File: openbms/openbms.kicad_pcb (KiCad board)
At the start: 4 copper layers, 68.4 x 52.4 mm, 210 parts, among them J1 3-pin JST connector, J2 TagConnect_TC2030, J3 8-pin JST connector, J4 2-pin JST connector, J5 XT60PW-M connector, J6 XT60PW-F connector, J7 7-pin JST connector, Q1 NTMFS5C612NLT1G, Q2 NTMFS5C612NLT1G, Q3 BSS84AKW,115, Q4 2N7002KW, Q5 2N7002KW, Q6 BSS84AKW,115, Q7 2N7002KW, U1 DMP68D1LVQ-7, U10 DMP68D1LVQ-7, U11 DMN601VK-7, U12 DMN601VK-7, U13 DMN601VK-7, U14 DMN601VK-7, U15 STM32L431CCUx, U16 TCAN3413DRBR, U17 32kbit EEPROM memory, U18 DMP68D1LVQ-7, U19 TPS12000QDGXRQ1, U2 DMP68D1LVQ-7, U20 LMZM23600V3, U3 DMN601VK-7, U4 DMP68D1LVQ-7, U5 ADS131M08xPBS, U6 DMP68D1LVQ-7, U7 DMN601VK-7, U8 DMP68D1LVQ-7, U9 DMP68D1LVQ-7, Y1 8.192MHz, Y2 8MHz

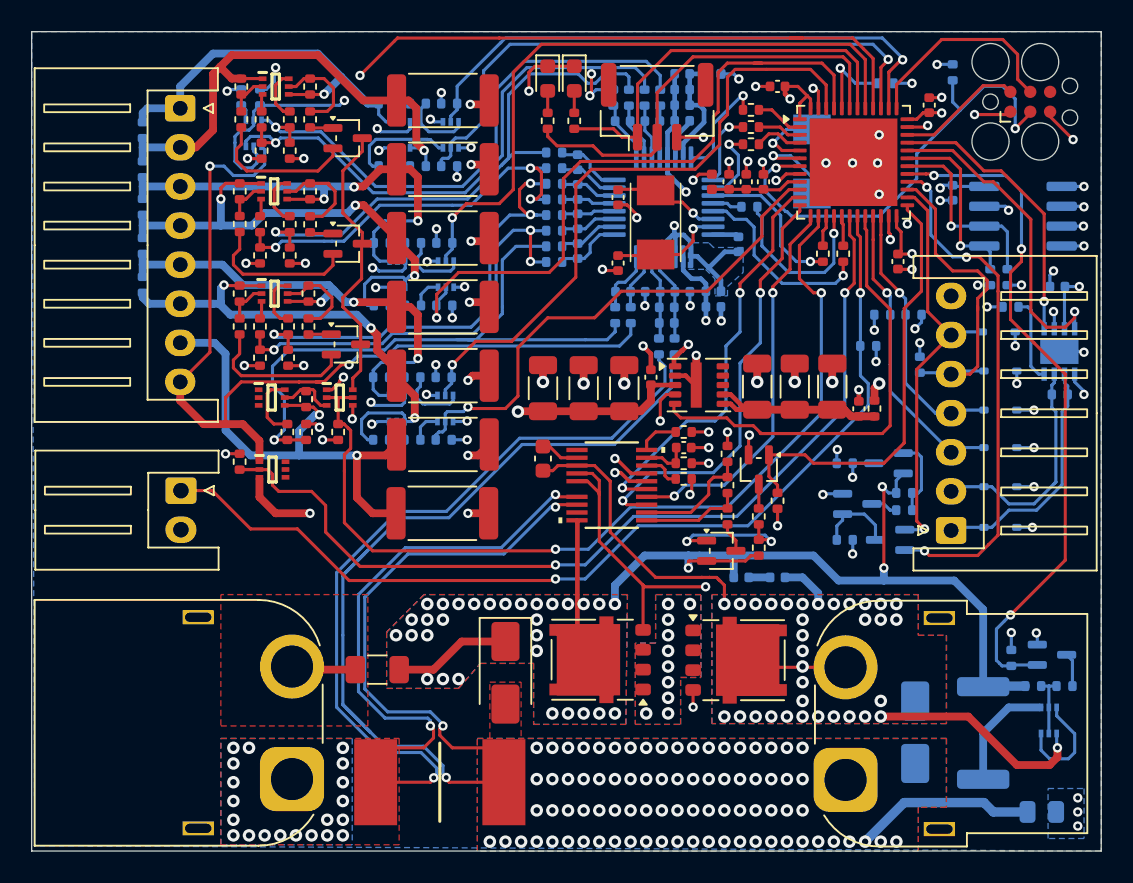
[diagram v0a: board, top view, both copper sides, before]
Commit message: Footprints for pmos/nmos and pmos/pmos packages fixed, charger detection added, pwr_gd and flt_gd lines removed
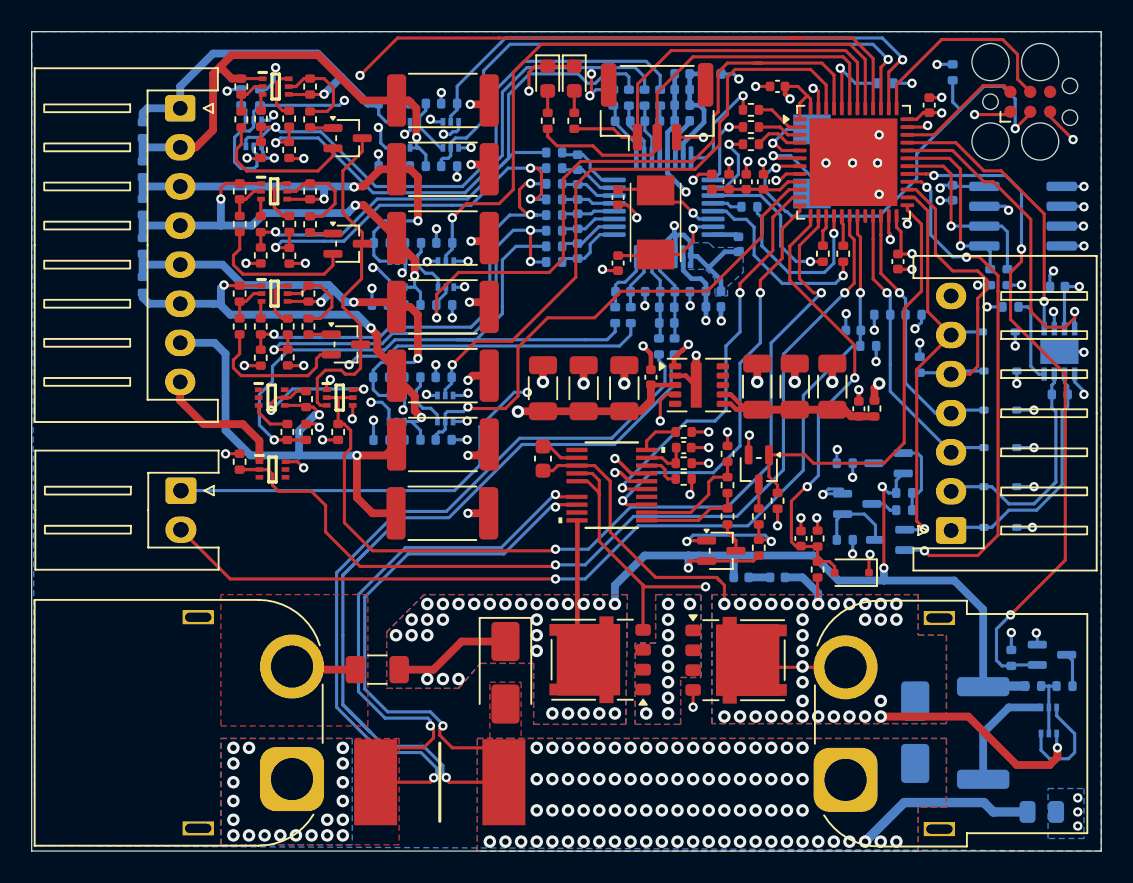
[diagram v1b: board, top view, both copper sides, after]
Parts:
- added C35: 10n, Capacitor_SMD:C_0402_1005Metric, B.Cu at (116.4, 53.3)
- added C44: 10n, Capacitor_SMD:C_0402_1005Metric, F.Cu at (113.0, 66.6)
- added D15: BAT54J, Diode_SMD:D_SOD-323F, F.Cu at (116.3, 68.8)
- added R116: 100k, Resistor_SMD:R_0402_1005Metric, F.Cu at (114.1, 68.6)
- added R118: 10k, Resistor_SMD:R_0402_1005Metric, F.Cu at (114.1, 66.6)
- Q1, Q2: footprint custom_library:ONSemi_SO-8FL_488AA -> Package_SO:ONSemi_SO-8FL_488AA
- U15: footprint custom_library:QFN-48-1EP_7x7mm_P0.5mm_EP5.6x5.6mm -> Package_DFN_QFN:QFN-48-1EP_7x7mm_P0.5mm_EP5.6x5.6mm
- U16: footprint custom_library:SON65P300X300X100-9N-D -> custom_library:TCAN3413DRBR
- U5: footprint custom_library:TQFP-32_5x5mm_P0.5mm -> Package_QFP:TQFP-32_5x5mm_P0.5mm
- moved R35 2.12 mm to (86.1, 51.7), turned to 0 degrees
- moved R63 2.00 mm to (88.2, 60.3), turned to 0 degrees
- moved R65 1.98 mm to (86.2, 60.4), turned to 0 degrees
- moved R31 1.96 mm to (88.2, 51.7), turned to 0 degrees
- moved R36 1.87 mm to (80.3, 48.6)
- moved R27 1.87 mm to (80.3, 46.5)
- moved R28 1.85 mm to (78.5, 46.5)
- moved R37 1.85 mm to (78.5, 48.5)
- moved R13 1.84 mm to (78.5, 39.8)
- moved R16 1.84 mm to (78.5, 41.8)
- moved R60 1.78 mm to (80.2, 55.1)
- moved R56 1.78 mm to (80.2, 53.1)
- moved R12 1.76 mm to (80.3, 39.8)
- moved R15 1.76 mm to (80.3, 41.8)
- moved R57 1.75 mm to (78.5, 53.1)
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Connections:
- net /Battery/BATT_PWR_VCC renamed /FETs/BATT_PWR_VCC
- J4 pad 1: /MCU/NTC -> +3V3
- J4 pad 2: GND -> /MCU/NTC
- R15 pad 1: GND -> GND_BATT_CELL
- R16 pad 1: GND -> GND_BATT_CELL
- R36 pad 1: GND -> GND_BATT_CELL
- R37 pad 1: GND -> GND_BATT_CELL
- R60 pad 1: GND -> GND_BATT_CELL
- R61 pad 1: GND -> GND_BATT_CELL
- R73 pad 1: GND -> GND_BATT_CELL
- R77 pad 1: GND -> GND_BATT_CELL
- U1 pad 3: Net-(R10-Pad2) -> Net-(R11-Pad2)
- U1 pad 6: Net-(R11-Pad2) -> Net-(R10-Pad2)
- U10 pad 3: unconnected-(U10-Pad3) -> Net-(R69-Pad2)
- U10 pad 6: Net-(R69-Pad2) -> unconnected-(U10-Pad6)
- U11 pad 3: Net-(R66-Pad2) -> Net-(D1-K)
- U11 pad 6: Net-(D1-K) -> Net-(R66-Pad2)
- U12 pad 3: Net-(R64-Pad1) -> Net-(R65-Pad1)
- U12 pad 6: Net-(R65-Pad1) -> Net-(R64-Pad1)
- U13 pad 3: Net-(R74-Pad1) -> unconnected-(U13-Pad3)
- U13 pad 6: unconnected-(U13-Pad6) -> Net-(R74-Pad1)
- U14 pad 3: /ADC/CELL_6_M -> /ADC/CELL_7_M
- U14 pad 6: /ADC/CELL_7_M -> /ADC/CELL_6_M
- U15 pad 13: /FETs/DRV_FLT_GD -> /FETs/CHG_PRES
- U15 pad 20: /MCU/PWR_PG -> unconnected-(U15-PB2-Pad20)
- U19 pad 4: /FETs/DRV_FLT_GD -> unconnected-(U19-FLT_GD-Pad4)
- U2 pad 3: Net-(R12-Pad2) -> Net-(R13-Pad2)
- U2 pad 6: Net-(R13-Pad2) -> Net-(R12-Pad2)
- U20 pad 5: /MCU/PWR_PG -> unconnected-(U20-PG-Pad5)
- U3 pad 3: Net-(R6-Pad1) -> Net-(R7-Pad1)
- U3 pad 6: Net-(R7-Pad1) -> Net-(R6-Pad1)
- U4 pad 3: Net-(R27-Pad2) -> Net-(R28-Pad2)
- U4 pad 6: Net-(R28-Pad2) -> Net-(R27-Pad2)
- U6 pad 3: Net-(R41-Pad2) -> Net-(R42-Pad2)
- U6 pad 6: Net-(R42-Pad2) -> Net-(R41-Pad2)
- U7 pad 3: Net-(R34-Pad1) -> Net-(R35-Pad1)
- U7 pad 6: Net-(R35-Pad1) -> Net-(R34-Pad1)
- U8 pad 3: Net-(R56-Pad2) -> Net-(R57-Pad2)
- U8 pad 6: Net-(R57-Pad2) -> Net-(R56-Pad2)
- U9 pad 3: Net-(R67-Pad2) -> Net-(R68-Pad2)
- U9 pad 6: Net-(R68-Pad2) -> Net-(R67-Pad2)
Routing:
- net +3V3: track 157.3 -> 200.9 mm, vias 18 -> 20
- net /FETs/CHG_PRES: track 0.00 -> 29.3 mm, vias 0 -> 2
- net /MCU/PWR_PG: track 29.2 -> 0.00 mm
- net /FETs/DRV_FLT_GD: track 24.8 -> 0.00 mm, vias 2 -> 0
- net GND_BATT_CELL: track 58.8 -> 80.9 mm, vias 2 -> 10
- net Net-(R35-Pad1): track 1.99 -> 9.42 mm, vias 0 -> 2
- net Net-(R65-Pad1): track 2.05 -> 9.41 mm, vias 0 -> 2
- net Net-(R66-Pad2): track 3.62 -> 10.2 mm, vias 0 -> 2
- net GND: track 121.3 -> 117.2 mm, vias 95 -> 90
- net Net-(D1-K): track 18.3 -> 22.2 mm
- net /ADC/CELL_4: track 33.5 -> 29.8 mm
- net /ADC/CELL_2: track 32.4 -> 29.2 mm
- net Net-(R57-Pad2): track 3.45 -> 1.11 mm
- net Net-(R13-Pad2): track 3.30 -> 1.09 mm
- net Net-(R27-Pad2): track 1.12 -> 3.30 mm
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
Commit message: Resistor dividers updated and put to 0.1% tolerance
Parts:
- R12, R13, R27, R28, R56, R57, R69: value 68k -> 68k,0.1%
- R15, R16, R36, R37, R60, R61, R73: value 3.3k -> 2k,0.1%
- R17, R20, R23, R24, R26, R32, R33, R43, R45, R48, R51, R55, R59: value 1k -> 1k,0.1%
- R77: value 3.3k -> 330R,0.1%
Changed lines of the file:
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@@
 			)
 		)
-		(property "Value" "3.3k"
+		(property "Value" "2k,0.1%"
 			(at 0 1.17 90)
 			(layer "F.Fab")
@@
 			)
 		)
-		(property "Manufacturer_Part_Number" "ERA-2AEB332X"
+		(property "Manufacturer_Part_Number" "RT0402BRD072KL"
 			(at 0 0 270)
 			(unlocked yes)
@@
 			)
 		)
-		(property "Value" "68k"
+		(property "Value" "68k,0.1%"
 			(at 0 1.17 90)
 			(layer "F.Fab")
@@
 			)
 		)
-		(property "Manufacturer_Part_Number" "RMCF0402FT68K0"
+		(property "Manufacturer_Part_Number" "RT0402BRD0768KL"
 			(at 0 0 90)
 			(unlocked yes)
@@
 			)
 		)
-		(property "Value" "3.3k"
+		(property "Value" "2k,0.1%"
 			(at 0 1.17 90)
 			(layer "F.Fab")
@@
 			)
 		)
-		(property "Manufacturer_Part_Number" "ERA-2AEB332X"
+		(property "Manufacturer_Part_Number" "RT0402BRD072KL"
 			(at 0 0 90)
 			(unlocked yes)
@@
 			)
 		)
-		(property "Value" "68k"
+		(property "Value" "68k,0.1%"
 			(at 0 1.17 90)
 			(layer "F.Fab")
@@
 			)
 		)
-		(property "Manufacturer_Part_Number" "RMCF0402FT68K0"
+		(property "Manufacturer_Part_Number" "RT0402BRD0768KL"
 			(at 0 0 90)
 			(unlocked yes)
@@
 			)
 		)
-		(property "Value" "3.3k"
+		(property "Value" "2k,0.1%"
 			(at 0 1.17 90)
 			(layer "F.Fab")
@@
 			)
 		)
-		(property "Manufacturer_Part_Number" "ERA-2AEB332X"
+		(property "Manufacturer_Part_Number" "RT0402BRD072KL"
 			(at 0 0 90)
 			(unlocked yes)
@@
 			)
 		)
-		(property "Value" "3.3k"
+		(property "Value" "2k,0.1%"
 			(at 0 1.17 90)
 			(layer "F.Fab")
@@
 			)
 		)
-		(property "Manufacturer_Part_Number" "ERA-2AEB332X"
+		(property "Manufacturer_Part_Number" "RT0402BRD072KL"
 			(at 0 0 90)
 			(unlocked yes)
@@
 			)
 		)
-		(property "Value" "68k"
+		(property "Value" "68k,0.1%"
 			(at 0 1.17 90)
 			(layer "F.Fab")
@@
 			)
 		)
-		(property "Manufacturer_Part_Number" "RMCF0402FT68K0"
+		(property "Manufacturer_Part_Number" "RT0402BRD0768KL"
 			(at 0 0 90)
 			(unlocked yes)
@@
 			)
 		)
-		(property "Value" "3.3k"
+		(property "Value" "2k,0.1%"
 			(at 0 1.17 90)
 			(layer "F.Fab")
@@
 			)
 		)
-		(property "Manufacturer_Part_Number" "ERA-2AEB332X"
+		(property "Manufacturer_Part_Number" "RT0402BRD072KL"
 			(at 0 0 90)
 			(unlocked yes)
@@
 			)
 		)
-		(property "Value" "3.3k"
+		(property "Value" "2k,0.1%"
 			(at 0 1.17 90)
 			(layer "F.Fab")
@@
 			)
 		)
-		(property "Manufacturer_Part_Number" "ERA-2AEB332X"
+		(property "Manufacturer_Part_Number" "RT0402BRD072KL"
 			(at 0 0 90)
 			(unlocked yes)
@@
 			)
 		)
-		(property "Value" "68k"
+		(property "Value" "68k,0.1%"
 			(at 0 1.17 90)
 			(layer "F.Fab")
@@
 			)
 		)
-		(property "Manufacturer_Part_Number" "RMCF0402FT68K0"
+		(property "Manufacturer_Part_Number" "RT0402BRD0768KL"
 			(at 0 0 90)
 			(unlocked yes)
@@
 			)
 		)
-		(property "Value" "68k"
+		(property "Value" "68k,0.1%"
 			(at 0 1.17 90)
 			(layer "F.Fab")
@@
 			)
 		)
-		(property "Manufacturer_Part_Number" "RMCF0402FT68K0"
+		(property "Manufacturer_Part_Number" "RT0402BRD0768KL"
 			(at 0 0 90)
 			(unlocked yes)
@@
 			)
 		)
-		(property "Value" "3.3k"
+		(property "Value" "2k,0.1%"
 			(at 0 1.17 90)
 			(layer "F.Fab")
@@
 			)
 		)
-		(property "Manufacturer_Part_Number" "ERA-2AEB332X"
+		(property "Manufacturer_Part_Number" "RT0402BRD072KL"
 			(at 0 0 90)
 			(unlocked yes)
@@
 			)
 		)
-		(property "Value" "68k"
+		(property "Value" "68k,0.1%"
 			(at 0.845 1.17 90)
 			(layer "F.Fab")
@@
 			)
 		)
-		(property "Manufacturer_Part_Number" "RMCF0402FT68K0"
+		(property "Manufacturer_Part_Number" "RT0402BRD0768KL"
 			(at 0 0 90)
 			(unlocked yes)
@@
 			)
 		)
-		(property "Value" "68k"
+		(property "Value" "68k,0.1%"
 			(at 0 1.17 90)
 			(layer "F.Fab")
@@
 			)
 		)
-		(property "Manufacturer_Part_Number" "RMCF0402FT68K0"
+		(property "Manufacturer_Part_Number" "RT0402BRD0768KL"
 			(at 0 0 90)
 			(unlocked yes)
@@
 			)
 		)
-		(property "Value" "1k"
+		(property "Value" "1k,0.1%"
 			(at 0 -1.17 90)
 			(layer "B.Fab")
@@
 			)
 		)
-		(property "Manufacturer_Part_Number" "RMCF0402FT1K00"
+		(property "Manufacturer_Part_Number" "RT0402BRD071KL"
 			(at 0 0 90)
 			(unlocked yes)
@@
 			)
 		)
-		(property "Value" "1k"
+		(property "Value" "1k,0.1%"
 			(at 0 -1.17 0)
 			(layer "B.Fab")
@@
 			)
 		)
-		(property "Manufacturer_Part_Number" "RMCF0402FT1K00"
+		(property "Manufacturer_Part_Number" "RT0402BRD071KL"
 			(at 0 0 180)
 			(unlocked yes)
@@
 			)
 		)
-		(property "Value" "1k"
+		(property "Value" "1k,0.1%"
 			(at 0 -1.17 0)
 			(layer "B.Fab")
@@
 			)
 		)
-		(property "Manufacturer_Part_Number" "RMCF0402FT1K00"
+		(property "Manufacturer_Part_Number" "RT0402BRD071KL"
 			(at 0 0 180)
 			(unlocked yes)
@@
 			)
 		)
-		(property "Value" "1k"
+		(property "Value" "1k,0.1%"
 			(at 0 -1.17 90)
 			(layer "B.Fab")
@@
 			)
 		)
-		(property "Manufacturer_Part_Number" "RMCF0402FT1K00"
+		(property "Manufacturer_Part_Number" "RT0402BRD071KL"
 			(at 0 0 90)
 			(unlocked yes)
@@
 			)
 		)
-		(property "Value" "3.3k"
+		(property "Value" "330R,0.1%"
 			(at 0 -1.17 90)
 			(layer "B.Fab")
@@
 			)
 		)
-		(property "Manufacturer_Part_Number" "ERA-2AEB332X"
+		(property "Manufacturer_Part_Number" "RT0402BRD07330RL"
 			(at 0 0 90)
 			(unlocked yes)
@@
 			)
 		)
-		(property "Value" "1k"
+		(property "Value" "1k,0.1%"
 			(at 0 -1.17 0)
 			(layer "B.Fab")
@@
 			)
 		)
-		(property "Manufacturer_Part_Number" "RMCF0402FT1K00"
+		(property "Manufacturer_Part_Number" "RT0402BRD071KL"
 			(at 0 0 180)
 			(unlocked yes)
@@
 			)
 		)
-		(property "Value" "1k"
+		(property "Value" "1k,0.1%"
 			(at 0 -1.17 0)
 			(layer "B.Fab")
@@
 			)
 		)
-		(property "Manufacturer_Part_Number" "RMCF0402FT1K00"
+		(property "Manufacturer_Part_Number" "RT0402BRD071KL"
 			(at 0 0 180)
 			(unlocked yes)
@@
 			)
 		)
-		(property "Value" "1k"
+		(property "Value" "1k,0.1%"
 			(at 0 -1.17 0)
 			(layer "B.Fab")
@@
 			)
 		)
-		(property "Manufacturer_Part_Number" "RMCF0402FT1K00"
+		(property "Manufacturer_Part_Number" "RT0402BRD071KL"
 			(at 0 0 180)
 			(unlocked yes)
@@
 			)
 		)
-		(property "Value" "1k"
+		(property "Value" "1k,0.1%"
 			(at 0 -1.17 90)
 			(layer "B.Fab")
@@
 			)
 		)
-		(property "Manufacturer_Part_Number" "RMCF0402FT1K00"
+		(property "Manufacturer_Part_Number" "RT0402BRD071KL"
 			(at 0 0 90)
 			(unlocked yes)
@@
 			)
 		)
-		(property "Value" "1k"
+		(property "Value" "1k,0.1%"
 			(at 0 -1.17 0)
 			(layer "B.Fab")
@@
 			)
 		)
-		(property "Manufacturer_Part_Number" "RMCF0402FT1K00"
+		(property "Manufacturer_Part_Number" "RT0402BRD071KL"
 			(at 0 0 180)
 			(unlocked yes)
@@
 			)
 		)
-		(property "Value" "1k"
+		(property "Value" "1k,0.1%"
 			(at 0 -1.17 90)
 			(layer "B.Fab")
@@
 			)
 		)
-		(property "Manufacturer_Part_Number" "RMCF0402FT1K00"
+		(property "Manufacturer_Part_Number" "RT0402BRD071KL"
 			(at 0 0 270)
 			(unlocked yes)
@@
 			)
 		)
-		(property "Value" "1k"
+		(property "Value" "1k,0.1%"
 			(at 0 -1.17 0)
 			(layer "B.Fab")
@@
 			)
 		)
-		(property "Manufacturer_Part_Number" "RMCF0402FT1K00"
+		(property "Manufacturer_Part_Number" "RT0402BRD071KL"
 			(at 0 0 180)
 			(unlocked yes)
@@
 			)
 		)
-		(property "Value" "1k"
+		(property "Value" "1k,0.1%"
 			(at 0 -1.17 90)
 			(layer "B.Fab")
@@
 			)
 		)
-		(property "Manufacturer_Part_Number" "RMCF0402FT1K00"
+		(property "Manufacturer_Part_Number" "RT0402BRD071KL"
 			(at 0 0 90)
 			(unlocked yes)
@@
 			)
 		)
-		(property "Value" "1k"
+		(property "Value" "1k,0.1%"
 			(at 0 -1.17 0)
 			(layer "B.Fab")
@@
 			)
 		)
-		(property "Manufacturer_Part_Number" "RMCF0402FT1K00"
+		(property "Manufacturer_Part_Number" "RT0402BRD071KL"
 			(at 0 0 180)
 			(unlocked yes)

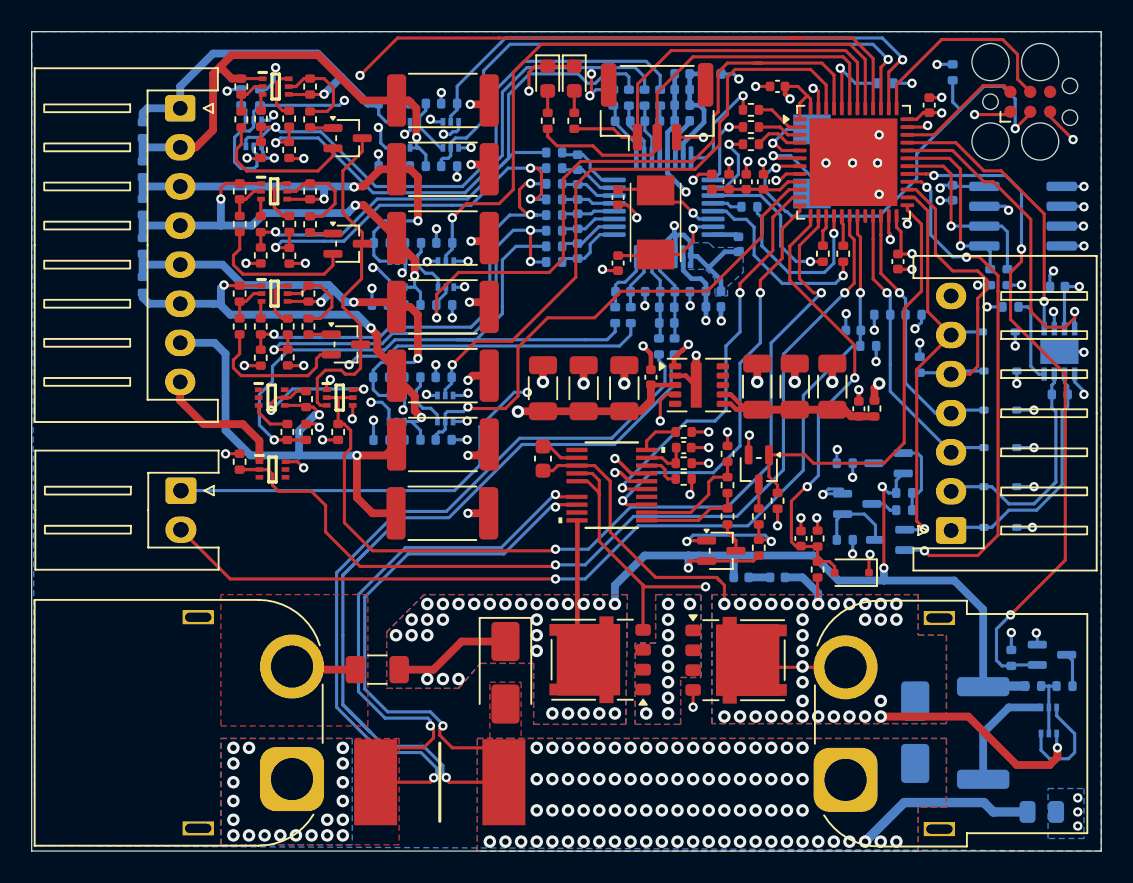
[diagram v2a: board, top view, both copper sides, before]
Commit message: Option to shortcut current ADC sensor added
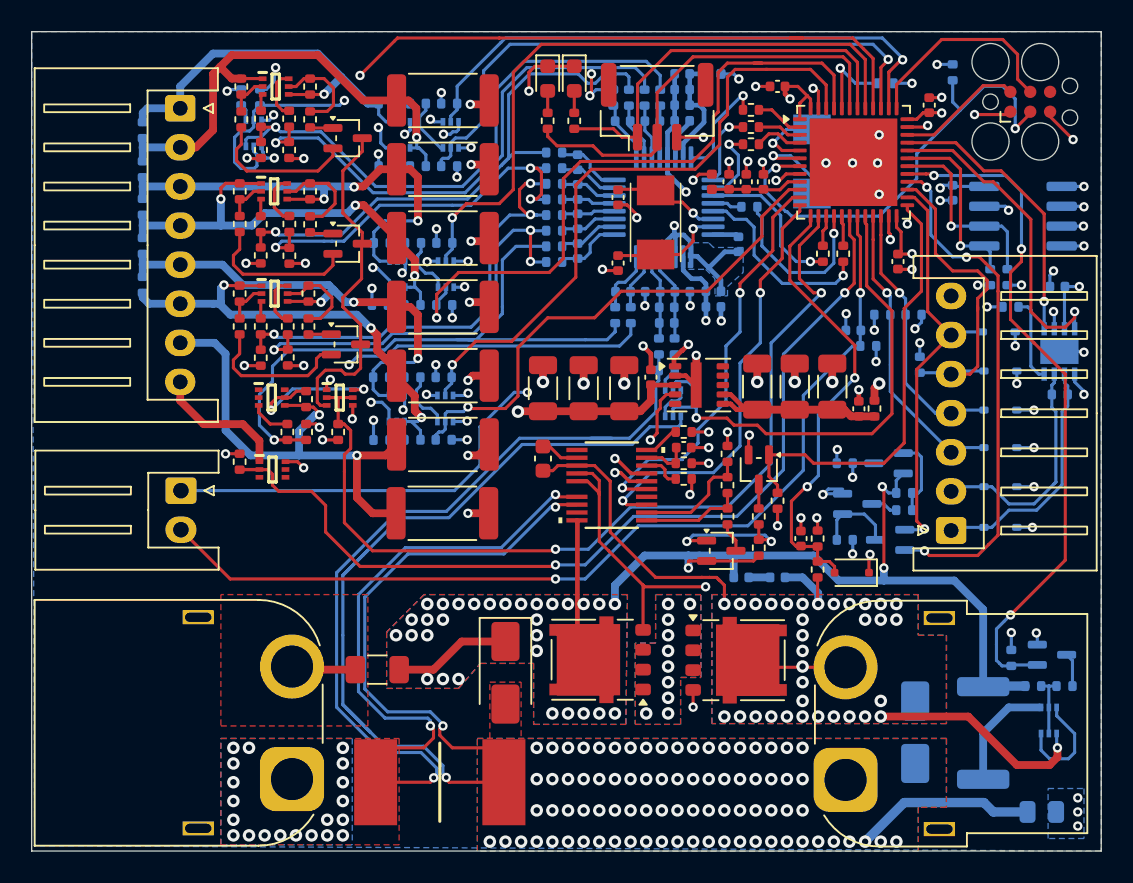
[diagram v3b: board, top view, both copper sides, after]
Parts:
- added R119: 100k, Resistor_SMD:R_0402_1005Metric, B.Cu at (104.5, 55.9)
- added U22: DMN601VK-7, custom_library:SOTFL50P162X60-6N, B.Cu at (104.8, 58.0)
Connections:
- R5 pad 1: SYS_GND -> Net-(R119-Pad2)
- U15 pad 20: unconnected-(U15-PB2-Pad20) -> /ADC/CURR_CAL
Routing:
- net /ADC/CURR_CAL: track 0.00 -> 32.8 mm, vias 0 -> 1
- net Net-(R119-Pad2): track 0.00 -> 2.55 mm
- net Net-(U22-Pad3): track 0.00 -> 2.32 mm
- net SYS_GND: track 107.7 -> 105.6 mm
- net /ADC/BATT_CS_POS: track 86.2 -> 87.9 mm
- net Net-(Q6-D): track 19.2 -> 20.0 mm

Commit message: Button for quick enable added
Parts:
- added C45: 100n, Capacitor_SMD:C_0402_1005Metric, B.Cu at (119.0, 60.0)
- added SW1: SW_Push, custom_library:435451019820, F.Cu at (127.8, 45.8)
- Q1, Q2: footprint Package_SO:ONSemi_SO-8FL_488AA -> custom_library:ONSemi_SO-8FL_488AA
- U15: footprint Package_DFN_QFN:QFN-48-1EP_7x7mm_P0.5mm_EP5.6x5.6mm -> custom_library:QFN-48-1EP_7x7mm_P0.5mm_EP5.6x5.6mm
- U5: footprint Package_QFP:TQFP-32_5x5mm_P0.5mm -> custom_library:TQFP-32_5x5mm_P0.5mm
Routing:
- net Net-(Q7-D): track 1.72 -> 47.6 mm, vias 0 -> 1
- net GND: track 117.2 -> 121.7 mm, vias 90 -> 93
- net Net-(Q6-G): track 5.14 -> 6.29 mm
- net /MCU/CAN_RX: track 20.6 -> 21.3 mm
- net /FETs/DRV_PRE_FET_EN: track 44.1 -> 44.7 mm

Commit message: FET driver EN and OV pin voltage levels fixed
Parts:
- added R117: 10k, Resistor_SMD:R_0402_1005Metric, F.Cu at (107.1, 63.2)
- R95: value 226k -> 261k
- R97: value 7.23k -> 137k
- moved R97 2.32 mm to (107.1, 65.2)
- moved R99 1.97 mm to (108.3, 63.2)
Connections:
- R95 pad 2: Net-(U19-EN/UVLO) -> Net-(U19-OV)
- R97 pad 1: Net-(U19-EN/UVLO) -> Net-(Q3-D)
- R97 pad 2: Net-(U19-OV) -> Net-(U19-EN/UVLO)
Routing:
- net Net-(U19-OV): track 7.56 -> 9.19 mm, vias 0 -> 2
- net Net-(Q3-D): track 1.91 -> 3.16 mm
- net Net-(U19-EN/UVLO): track 6.47 -> 5.25 mm
- net GND: track 121.7 -> 123.0 mm
